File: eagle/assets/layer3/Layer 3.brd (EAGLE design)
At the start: 196 x 158 mm, 82 parts, among them Q2 AO3402, X1 SM06B-SRSS-TB, Y1 8MHz

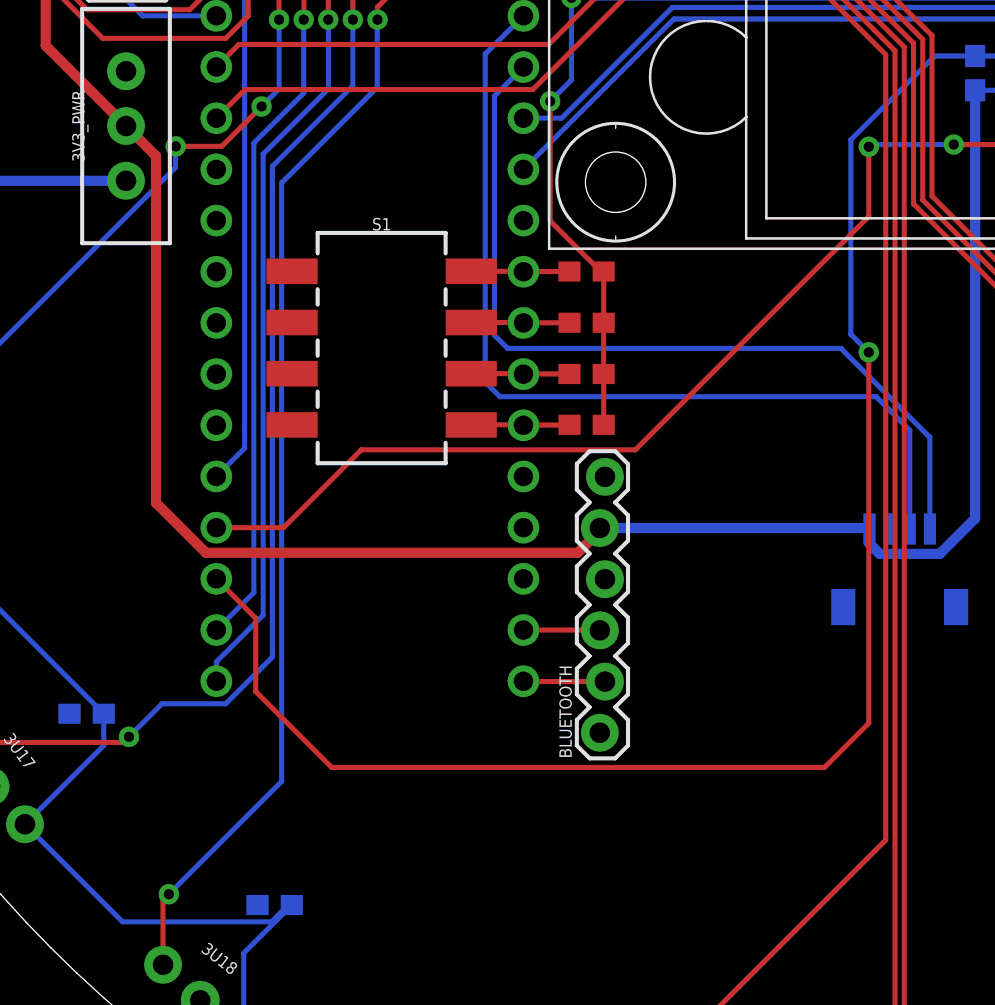
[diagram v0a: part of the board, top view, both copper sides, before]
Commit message: 🚀🚀🚀 Edited Layer 3 and 4 Changed the positioning of the BT Module Change the positioning of the connectors
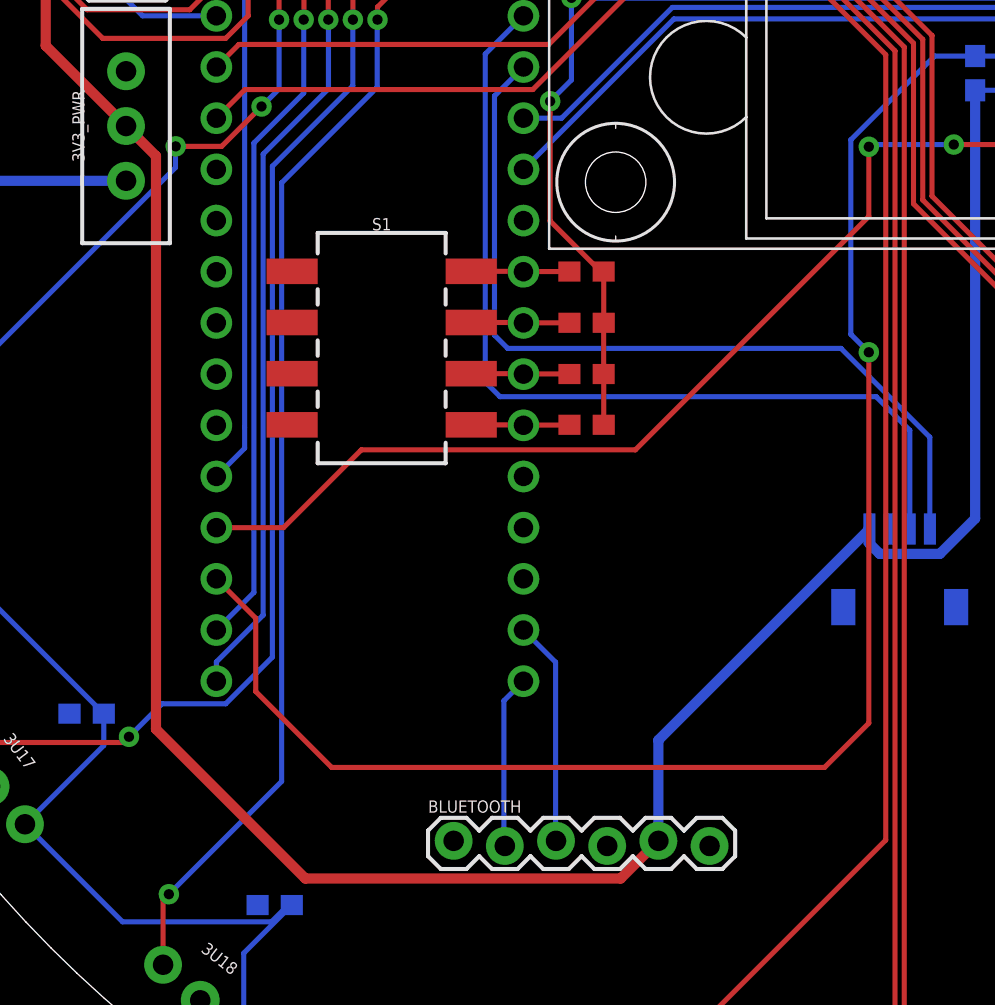
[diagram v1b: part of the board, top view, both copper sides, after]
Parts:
- moved BLUETOOTH 9.02 mm to (-22.5, -37.0), turned to 0 degrees
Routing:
- net 3.3V: track 112.1 -> 134.9 mm
- net TX_BT: track 3.80 -> 11.1 mm
- net RX_BT: track 4.05 -> 8.60 mm
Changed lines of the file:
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@@
 </layers>
 <board>
-<fusionsync huburn="a.YnVzaW5lc3M6Z21haWwxNDMxNzc3" projecturn="a.YnVzaW5lc3M6Z21haWwxNDMxNzc3IzIwMjIwMTE1NDg1NTYyMzgx" f3durn="urn:adsk.wipprod:dm.lineage:XRrs2BLERA6S8rtlune0tg" pcbguid="4256a642-5b2c-49b0-9c3c-d98547ff719c" lastpulledtime="" lastsyncedchangeguid="" latestrevisionid="a48e7467-8cc9-48b6-9e54-6847a9677708" lastsyncedrevisionid="a48e7467-8cc9-48b6-9e54-6847a9677708" lastboardhashguid="303b5999-d3ac-b227-7182-65dbfc97586a" lastpushedtime="2022-01-15T04:54:14Z" linktopcb3d="true"/>
+<fusionsync huburn="a.YnVzaW5lc3M6Z21haWwxNDMxNzc3" projecturn="a.YnVzaW5lc3M6Z21haWwxNDMxNzc3IzIwMjIwMTE1NDg1NTYyMzgx" f3durn="urn:adsk.wipprod:dm.lineage:XRrs2BLERA6S8rtlune0tg" pcbguid="" lastpulledtime="" lastsyncedchangeguid="" latestrevisionid="99dcdaba-ee36-43fb-bf1c-f44e392e57b2" lastsyncedrevisionid="99dcdaba-ee36-43fb-bf1c-f44e392e57b2" lastboardhashguid="ce570c98-bab3-24c3-e4d3-7ff82e6ee8c1" lastpushedtime="2022-01-17T14:32:45Z" linktopcb3d="true"/>
 <plain>
 <circle x="-88.92016875" y="-27.259159375" radius="3.54114375" width="0.1524" layer="39"/>
@@
 <attribute name="VALUE" x="22.6385" y="3.3794125" size="0.6096" layer="27" font="vector" ratio="20" rot="R90" align="top-center"/>
 </element>
-<element name="BLUETOOTH" library="JH" library_urn="urn:adsk.eagle:library:6027132" package="HC-05" package3d_urn="urn:adsk.eagle:package:16970951/2" value="HC-05" x="-15.2623875" y="-31.63925" smashed="yes" rot="R90">
-<attribute name="NAME" x="-16.6593875" y="-32.90925" size="0.6096" layer="25" font="vector" ratio="20" rot="R90"/>
-<attribute name="VALUE" x="-12.9763875" y="-32.90925" size="0.6096" layer="27" font="vector" ratio="20" rot="R90"/>
+<element name="BLUETOOTH" library="JH" library_urn="urn:adsk.eagle:library:6027132" package="HC-05" package3d_urn="urn:adsk.eagle:package:16970951/2" value="HC-05" x="-22.51825" y="-37.0026125" smashed="yes">
+<attribute name="NAME" x="-23.78825" y="-35.6056125" size="0.6096" layer="25" font="vector" ratio="20"/>
+<attribute name="VALUE" x="-23.78825" y="-39.2886125" size="0.6096" layer="27" font="vector" ratio="20"/>
 </element>
 <element name="BOOT" library="MY-LIBRARY" library_urn="urn:adsk.eagle:library:11016882" package="MOMENTARY_SWITCH_4X3" package3d_urn="urn:adsk.eagle:package:11016890/3" value="MOMENTARY_SWITCH_4X3" x="25.79" y="14.42" smashed="yes" rot="R270">
@@
 <wire x1="-38.775909375" y1="-1.530290625" x2="-42.761975" y2="2.455775" width="0.508" layer="1"/>
 <wire x1="-42.761975" y1="2.455775" x2="-42.761975" y2="17.87276875" width="0.508" layer="1"/>
-<wire x1="-34.80991875" y1="-22.70786875" x2="-37.2900375" y2="-20.22775" width="0.508" layer="1"/>
-<wire x1="-15.2623875" y1="-21.47925" x2="-15.2623875" y2="-21.6129" width="0.508" layer="1"/>
-<wire x1="-15.2623875" y1="-21.6129" x2="-16.35735625" y2="-22.70786875" width="0.508" layer="1"/>
-<wire x1="-16.35735625" y1="-22.70786875" x2="-34.80991875" y2="-22.70786875" width="0.508" layer="1"/>
-<wire x1="-37.2900375" y1="-3.0161625" x2="-38.775909375" y2="-1.530290625" width="0.508" layer="1"/>
-<wire x1="-37.2900375" y1="-20.22775" x2="-37.2900375" y2="-3.0161625" width="0.508" layer="1"/>
+<wire x1="-38.775909375" y1="-1.530290625" x2="-37.2900375" y2="-3.0161625" width="0.508" layer="1"/>
 <wire x1="-1.900125" y1="-21.546" x2="-1.883" y2="-21.528875" width="0.508" layer="16"/>
 <wire x1="-1.373125" y1="-22.762875" x2="-1.892" y2="-22.244" width="0.508" layer="16"/>
@@
 <wire x1="3.36121875" y1="-21.00878125" x2="1.607125" y2="-22.762875" width="0.508" layer="16"/>
 <wire x1="3.36121875" y1="0.243825" x2="3.36121875" y2="-21.00878125" width="0.508" layer="16"/>
-<wire x1="-15.2623875" y1="-21.47925" x2="-1.932625" y2="-21.47925" width="0.508" layer="16"/>
-<wire x1="-1.932625" y1="-21.47925" x2="-1.883" y2="-21.528875" width="0.508" layer="16"/>
+<wire x1="-1.883" y1="-21.528875" x2="-1.932625" y2="-21.47925" width="0.508" layer="16"/>
+<wire x1="-12.35825" y1="-32.004125" x2="-12.35825" y2="-37.0026125" width="0.508" layer="16"/>
+<wire x1="-1.883" y1="-21.528875" x2="-12.35825" y2="-32.004125" width="0.508" layer="16"/>
+<wire x1="-37.2900375" y1="-31.4599625" x2="-29.879" y2="-38.871" width="0.508" layer="1"/>
+<wire x1="-29.879" y1="-38.871" x2="-14.2266375" y2="-38.871" width="0.508" layer="1"/>
+<wire x1="-14.2266375" y1="-38.871" x2="-12.35825" y2="-37.0026125" width="0.508" layer="1"/>
+<wire x1="-37.2900375" y1="-3.0161625" x2="-37.2900375" y2="-31.4599625" width="0.508" layer="1"/>
 </signal>
 <signal name="5V">
@@
 <contactref element="U$1" pad="32/A13"/>
 <contactref element="BLUETOOTH" pad="2"/>
-<wire x1="-15.0083875" y1="-29.09925" x2="-19.03585625" y2="-29.09925" width="0.254" layer="1"/>
-<wire x1="-19.03585625" y1="-29.09925" x2="-19.053640625" y2="-29.081465625" width="0.254" layer="1"/>
+<wire x1="-19.053640625" y1="-29.081465625" x2="-20.023640625" y2="-30.051465625" width="0.254" layer="16"/>
+<wire x1="-20.023640625" y1="-30.051465625" x2="-20.023640625" y2="-37.211221875" width="0.254" layer="16"/>
+<wire x1="-19.97825" y1="-37.2566125" x2="-20.023640625" y2="-37.211221875" width="0.254" layer="16"/>
 </signal>
 <signal name="TX_BT">
 <contactref element="U$1" pad="31/A12"/>
 <contactref element="BLUETOOTH" pad="3"/>
-<wire x1="-19.053640625" y1="-26.541465625" x2="-15.280171875" y2="-26.541465625" width="0.254" layer="1"/>
-<wire x1="-15.280171875" y1="-26.541465625" x2="-15.2623875" y2="-26.55925" width="0.254" layer="1"/>
+<wire x1="-17.4592375" y1="-28.13586875" x2="-17.4592375" y2="-36.981625" width="0.254" layer="16"/>
+<wire x1="-17.43825" y1="-37.0026125" x2="-17.4592375" y2="-36.981625" width="0.254" layer="16"/>
+<wire x1="-19.053640625" y1="-26.541465625" x2="-17.4592375" y2="-28.13586875" width="0.254" layer="16"/>
 </signal>
 <signal name="SERVO_HV">

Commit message: 🥰 Layer 3 Edits Changed oreintation of XH Connectors Shrunk the radius of IR Sensor
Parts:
- moved 3C4 14.1 mm to (46.4, 18.7), flipped to the top, turned to 22 degrees
- moved 3C20 13.4 mm to (-6.96, -49.5), flipped to the top, turned to 262 degrees
- moved 3C15 13.2 mm to (-49.6, -6.09), flipped to the top, turned to 187 degrees
- moved 3C21 13.2 mm to (6.09, -49.6), flipped to the top, turned to 277 degrees
- moved 3C3 13.2 mm to (49.6, 6.09), flipped to the top, turned to 7 degrees
- moved 3C9 13.2 mm to (-6.09, 49.6), flipped to the top, turned to 97 degrees
- moved 3C14 13.2 mm to (-49.5, 6.96), flipped to the top, turned to 172 degrees
- moved 3C2 13.2 mm to (49.5, -6.96), flipped to the top, turned to 352 degrees
- moved 3C8 13.2 mm to (6.96, 49.5), flipped to the top, turned to 82 degrees
- moved 3C12 13.2 mm to (-39.4, 30.8), flipped to the top, turned to 142 degrees
- moved 3C18 13.2 mm to (-30.8, -39.4), flipped to the top, turned to 232 degrees
- moved 3C24 13.2 mm to (39.4, -30.8), flipped to the top, turned to 322 degrees
- moved 3C6 13.2 mm to (30.8, 39.4), flipped to the top, turned to 52 degrees
- moved 3C16 13.2 mm to (-46.4, -18.7), flipped to the top, turned to 202 degrees
- moved 3C22 13.2 mm to (18.7, -46.4), flipped to the top, turned to 292 degrees
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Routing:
- net 3V3_SWITCH: track 627.2 -> 563.4 mm, vias 11 -> 12
- net GND: track 20.4 -> 9.08 mm, vias 4 -> 3
- net IR7: track 43.6 -> 37.0 mm, vias 2 -> 1
- net IR2: track 76.6 -> 71.1 mm, vias 6 -> 5
- net IR8: track 35.8 -> 30.8 mm, vias 2 -> 1
- net RX1_ST2: track 82.0 -> 86.9 mm
- net IR6: track 48.2 -> 43.9 mm, vias 2 -> 1
- net IR12: track 45.3 -> 41.3 mm, vias 2 -> 1
- net 3.3V: track 134.9 -> 131.0 mm
- net IR24: track 81.1 -> 77.4 mm, vias 0 -> 1
- net IR1: track 80.3 -> 77.0 mm, vias 4 -> 3
- net IR10: track 32.0 -> 28.8 mm, vias 2 -> 1
- net IR22: track 82.3 -> 79.0 mm, vias 0 -> 1
- net TX2_ST3: track 45.9 -> 42.8 mm
- net IR5: track 50.8 -> 47.7 mm, vias 2 -> 1
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
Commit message: 🦅
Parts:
- moved X1 1.55 mm to (5.62, 31.8), turned to 0 degrees
- turned 4TH_LAYER to 180 degrees
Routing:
- net GND: track 9.08 -> 0.00 mm, vias 3 -> 0
- net 3V3_SWITCH: track 563.4 -> 567.8 mm, vias 12 -> 11
- net SWDIO: track 22.1 -> 26.0 mm
- net IR7: track 37.0 -> 39.6 mm
- net SWCLK: track 22.6 -> 20.6 mm
- net TX2_ST3: track 42.8 -> 44.4 mm, vias 0 -> 2
- net RX1_ST2: track 86.9 -> 88.3 mm
- net RX2_ST3: track 40.1 -> 41.4 mm
- net TX1_ST2: track 84.3 -> 85.1 mm

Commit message: -
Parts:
- moved 3C4 14.1 mm to (41.3, 31.8), flipped to the bottom, turned to 180 degrees
- moved 3C20 13.4 mm to (6.38, -50.6), flipped to the bottom, turned to 7 degrees
- moved 3C15 13.2 mm to (-47.3, -19.1), flipped to the bottom, turned to 0 degrees
- moved 3C21 13.2 mm to (19.1, -47.3), flipped to the bottom, turned to 0 degrees
- moved 3C3 13.2 mm to (47.3, 19.1), flipped to the bottom, turned to 0 degrees
- moved 3C9 13.2 mm to (-19.1, 47.3), flipped to the bottom, turned to 0 degrees
- moved 3C14 13.2 mm to (-50.6, -6.22), flipped to the bottom, turned to 0 degrees
- moved 3C2 13.2 mm to (50.6, 6.22), flipped to the bottom, turned to 0 degrees
- moved 3C8 13.2 mm to (-6.22, 50.6), flipped to the bottom, turned to 0 degrees
- moved 3C12 13.2 mm to (-46.9, 19.9), flipped to the bottom, turned to 0 degrees
- moved 3C18 13.2 mm to (-19.9, -46.9), flipped to the bottom, turned to 0 degrees
- moved 3C24 13.2 mm to (46.9, -19.9), flipped to the bottom, turned to 0 degrees
- moved 3C6 13.2 mm to (19.9, 46.9), flipped to the bottom, turned to 120 degrees
- moved 3C16 13.2 mm to (-40.7, -30.7), flipped to the bottom, turned to 0 degrees
- moved 3C22 13.2 mm to (30.7, -40.7), flipped to the bottom, turned to 0 degrees
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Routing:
- net 3V3_SWITCH: track 567.8 -> 627.2 mm
- net GND: track 0.00 -> 20.4 mm, vias 0 -> 4
- net 3.3V: track 130.7 -> 112.1 mm
- net TX_BT: track 11.1 -> 3.80 mm
- net RX1_ST2: track 88.3 -> 82.0 mm
- net IR2: track 71.1 -> 76.6 mm, vias 5 -> 6
- net IR8: track 30.8 -> 35.8 mm, vias 1 -> 2
- net SWDIO: track 26.0 -> 21.3 mm
- net RX_BT: track 8.60 -> 4.05 mm
- net IR12: track 41.3 -> 45.3 mm, vias 1 -> 2
- net IR7: track 39.6 -> 43.6 mm, vias 1 -> 2
- net IR6: track 44.3 -> 48.2 mm, vias 1 -> 2
- net IR24: track 77.4 -> 81.1 mm, vias 1 -> 0
- net IR18: track 74.0 -> 77.5 mm, vias 1 -> 2
- net TX1_ST2: track 85.1 -> 81.7 mm, vias 4 -> 2
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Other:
- board size 196 x 158 mm -> 196 x 160.1 mm

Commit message: 💀 Almost died again thank god hv backup
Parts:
- moved 3C4 14.1 mm to (46.4, 18.7), flipped to the top, turned to 22 degrees
- moved 3C20 13.4 mm to (-6.96, -49.5), flipped to the top, turned to 262 degrees
- moved 3C15 13.2 mm to (-49.6, -6.09), flipped to the top, turned to 187 degrees
- moved 3C21 13.2 mm to (6.09, -49.6), flipped to the top, turned to 277 degrees
- moved 3C3 13.2 mm to (49.6, 6.09), flipped to the top, turned to 7 degrees
- moved 3C9 13.2 mm to (-6.09, 49.6), flipped to the top, turned to 97 degrees
- moved 3C14 13.2 mm to (-49.5, 6.96), flipped to the top, turned to 172 degrees
- moved 3C2 13.2 mm to (49.5, -6.96), flipped to the top, turned to 352 degrees
- moved 3C8 13.2 mm to (6.96, 49.5), flipped to the top, turned to 82 degrees
- moved 3C12 13.2 mm to (-39.4, 30.8), flipped to the top, turned to 142 degrees
- moved 3C18 13.2 mm to (-30.8, -39.4), flipped to the top, turned to 232 degrees
- moved 3C24 13.2 mm to (39.4, -30.8), flipped to the top, turned to 322 degrees
- moved 3C6 13.2 mm to (30.8, 39.4), flipped to the top, turned to 52 degrees
- moved 3C16 13.2 mm to (-46.4, -18.7), flipped to the top, turned to 202 degrees
- moved 3C22 13.2 mm to (18.7, -46.4), flipped to the top, turned to 292 degrees
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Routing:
- net 3V3_SWITCH: track 627.2 -> 563.4 mm, vias 11 -> 12
- net 3.3V: track 112.1 -> 131.0 mm
- net GND: track 20.4 -> 9.08 mm, vias 4 -> 3
- net TX_BT: track 3.80 -> 11.1 mm
- net IR7: track 43.6 -> 37.0 mm, vias 2 -> 1
- net IR2: track 76.6 -> 71.1 mm, vias 6 -> 5
- net IR8: track 35.8 -> 30.8 mm, vias 2 -> 1
- net RX1_ST2: track 82.0 -> 86.9 mm
- net RX_BT: track 4.05 -> 8.60 mm
- net IR6: track 48.2 -> 43.9 mm, vias 2 -> 1
- net IR12: track 45.3 -> 41.3 mm, vias 2 -> 1
- net IR24: track 81.1 -> 77.4 mm, vias 0 -> 1
- net IR1: track 80.3 -> 77.0 mm, vias 4 -> 3
- net IR10: track 32.0 -> 28.8 mm, vias 2 -> 1
- net IR22: track 82.3 -> 79.0 mm, vias 0 -> 1
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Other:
- board size 196 x 160.1 mm -> 196 x 158 mm

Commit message: fucked up
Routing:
- net SWDIO: track 22.1 -> 21.6 mm
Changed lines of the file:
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@@
 </layers>
 <board>
-<fusionsync huburn="a.YnVzaW5lc3M6Z21haWwxNDMxNzc3" projecturn="a.YnVzaW5lc3M6Z21haWwxNDMxNzc3IzIwMjIwMTE1NDg1NTYyMzgx" f3durn="urn:adsk.wipprod:dm.lineage:XRrs2BLERA6S8rtlune0tg" pcbguid="" lastpulledtime="" lastsyncedchangeguid="" latestrevisionid="3926b08f-832c-42fd-ab0e-15fb2e728c54" lastsyncedrevisionid="3926b08f-832c-42fd-ab0e-15fb2e728c54" lastboardhashguid="db1c863a-973b-28a7-95aa-0edf2f134072" lastpushedtime="2022-01-18T14:24:35Z" linktopcb3d="true"/>
+<fusionsync huburn="a.YnVzaW5lc3M6Z21haWwxNDMxNzc3" projecturn="a.YnVzaW5lc3M6Z21haWwxNDMxNzc3IzIwMjIwMTE1NDg1NTYyMzgx" f3durn="urn:adsk.wipprod:dm.lineage:XRrs2BLERA6S8rtlune0tg" pcbguid="" lastpulledtime="" lastsyncedchangeguid="" latestrevisionid="fa86db70-ce8d-47bf-9d5a-0212fa38592e" lastsyncedrevisionid="fa86db70-ce8d-47bf-9d5a-0212fa38592e" lastboardhashguid="a5d7cd8c-b1db-b74b-8178-91eda33b5f82" lastpushedtime="2022-01-19T10:09:03Z" linktopcb3d="true"/>
 <plain>
 <circle x="-88.92016875" y="-27.259159375" radius="3.54114375" width="0.1524" layer="39"/>
@@
 <wire x1="-8.536425" y1="21.778" x2="-6.183425" y2="21.778" width="0.254" layer="16"/>
 <wire x1="0.891575" y1="28.853" x2="4.45794375" y2="28.853" width="0.254" layer="16"/>
-<wire x1="7.546" y1="30.54805625" x2="7.046" y2="30.673" width="0.254" layer="16"/>
-<wire x1="7.043" y1="30.67" x2="7.046" y2="30.673" width="0.254" layer="16"/>
-<wire x1="4.45794375" y1="28.853" x2="6.27494375" y2="30.67" width="0.254" layer="16"/>
-<wire x1="6.27494375" y1="30.67" x2="7.043" y2="30.67" width="0.254" layer="16"/>
+<wire x1="6.27494375" y1="30.67" x2="4.45794375" y2="28.853" width="0.254" layer="16"/>
+<wire x1="7.046" y1="30.673" x2="7.043" y2="30.67" width="0.254" layer="16"/>
+<wire x1="7.043" y1="30.67" x2="6.27494375" y2="30.67" width="0.254" layer="16"/>
 </signal>
 <signal name="SWCLK">

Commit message: 🦅☠️
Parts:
- moved X1 1.55 mm to (5.62, 31.8), turned to 0 degrees
- turned 4TH_LAYER to 180 degrees
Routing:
- net GND: track 9.08 -> 0.00 mm, vias 3 -> 0
- net 3V3_SWITCH: track 563.4 -> 567.8 mm, vias 12 -> 11
- net SWDIO: track 21.6 -> 26.0 mm
- net IR7: track 37.0 -> 39.6 mm
- net SWCLK: track 22.6 -> 20.6 mm
- net TX2_ST3: track 42.8 -> 44.4 mm, vias 0 -> 2
- net RX1_ST2: track 86.9 -> 88.3 mm
- net RX2_ST3: track 40.1 -> 41.4 mm
- net TX1_ST2: track 84.3 -> 85.1 mm
